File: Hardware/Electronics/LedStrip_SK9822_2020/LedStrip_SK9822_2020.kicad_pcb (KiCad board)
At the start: 2 copper layers, 202.8 x 12 mm, 56 parts, among them J1 Conn_01x08

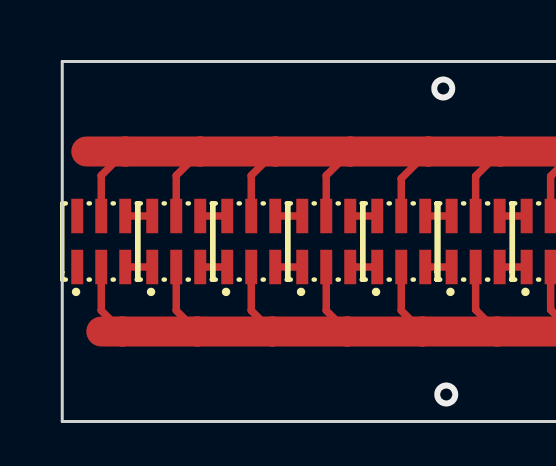
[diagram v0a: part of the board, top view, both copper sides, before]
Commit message: Rename SK9822 led strip project
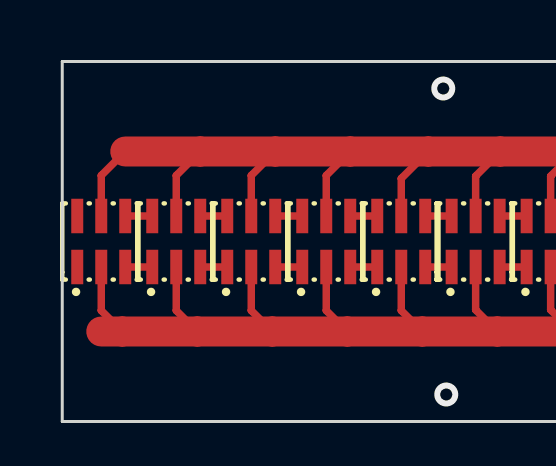
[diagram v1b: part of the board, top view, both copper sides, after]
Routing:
- net +5V: track 409.7 -> 408.4 mm
